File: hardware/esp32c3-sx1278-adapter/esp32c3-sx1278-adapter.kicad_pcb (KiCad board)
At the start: 2 copper layers, 24 x 55 mm, 4 parts, among them J1 Conn_01x08, J2 Conn_01x08, J3 Antenna, U2 SX1278_module

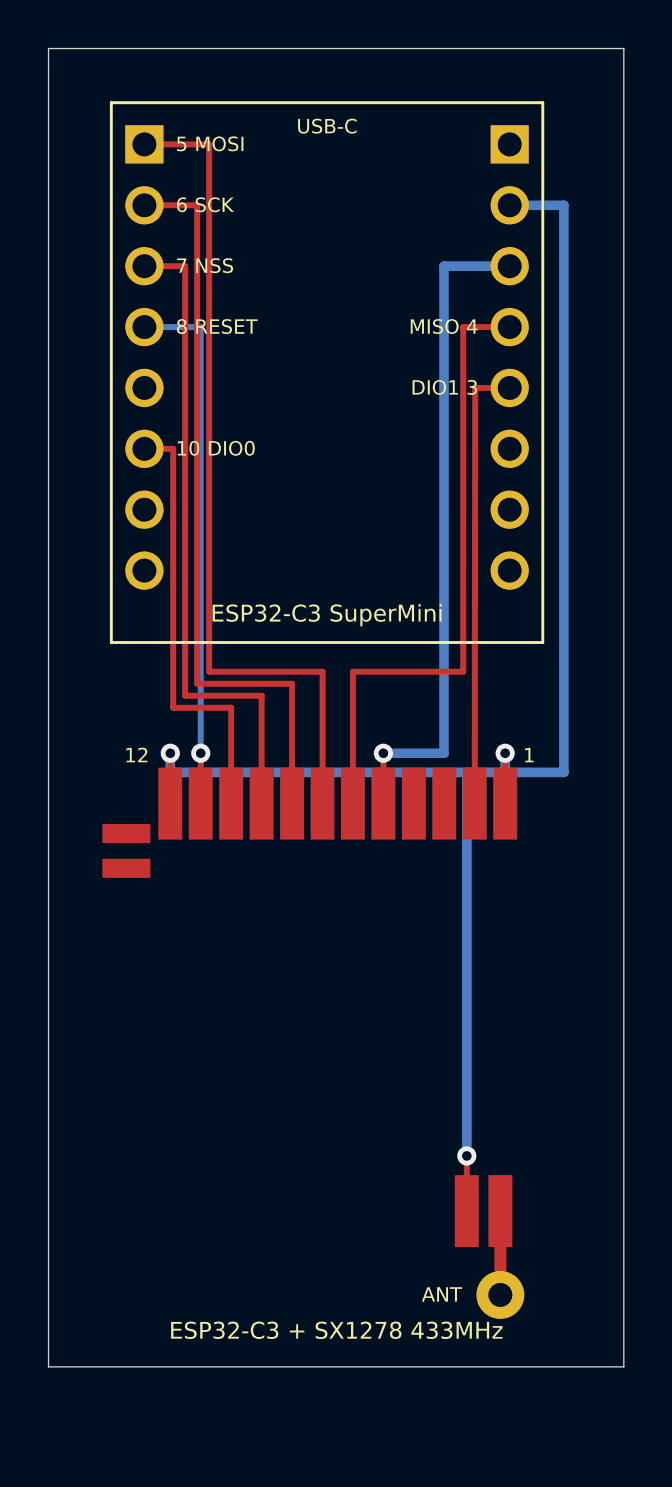
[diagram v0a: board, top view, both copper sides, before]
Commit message: Make the CC1101 adapter single-sided; add ESP32 pin names to silk
All tracks of the ESP32-C3 to CC1101 adapter now run on B.Cu (the
front keeps only the through-hole pad rings).  To make the eight nets
planar without jumpers the SuperMini lies on its side with USB-C off
the left edge, so its GPIO row sits above the socket and its power row
behind it; MISO and GDO2 go over the top of the power row and down the
left edge.  Board is 30 x 38 mm.

Both adapters now print the SuperMini's own pin names on the outer
side of each header row and the radio signal names on the inner side.
Layout plots now include B.Cu.

Co-Authored-By: Claude Fable 5.1 <noreply@anthropic.com>
Claude-Session: https://claude.ai/code/session_01JoGdh4Cg3VtTTDZi4gQuiN
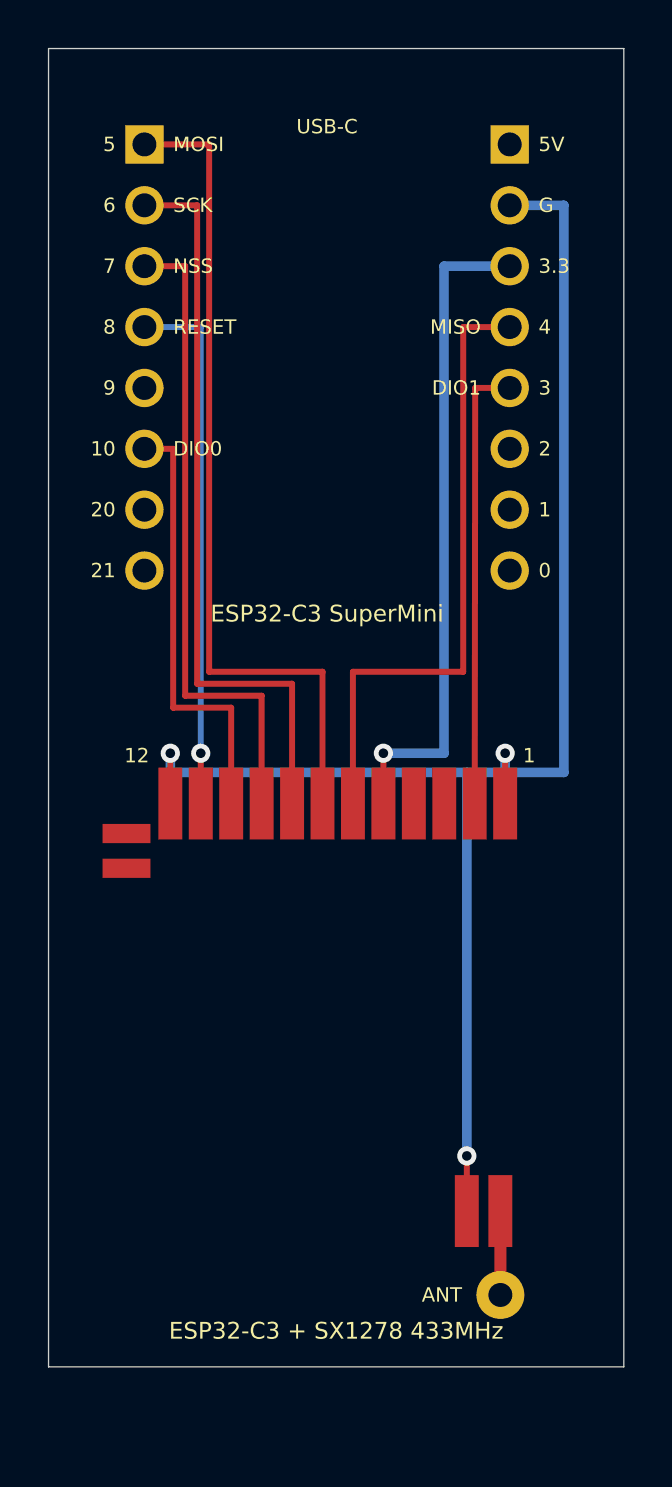
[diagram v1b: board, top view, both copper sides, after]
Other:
- board text added: "0"
- board text added: "1"
- board text added: "10"
- board text added: "2"
- board text added: "20"
- board text added: "21"
- board text added: "3"
- board text added: "3.3"
- board text added: "4"
- board text added: "5"
- board text added: "5V"
- board text added: "6"
- board text added: "7"
- board text added: "8"
- board text added: "9"
- board text added: "DIO0"
- board text added: "DIO1"
- board text added: "G"
- board text added: "MISO"
- board text added: "MOSI"
- board text added: "NSS"
- board text added: "RESET"
- board text added: "SCK"
- board text removed: "10 DIO0"
- board text removed: "5 MOSI"
- board text removed: "6 SCK"
- board text removed: "7 NSS"
- board text removed: "8 RESET"
- board text removed: "DIO1 3"
- board text removed: "MISO 4"
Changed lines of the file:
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@@
 		)
 		(fill no)
-		(layer "F.SilkS")
+		(layer "F.Fab")
 	)
 	(gr_rect
@@
 		)
 	)
-	(gr_text "5 MOSI"
-		(at 105.3 104 0)
-		(layer "F.SilkS")
-		(effects
-			(font
-				(size 0.6 0.6)
-				(thickness 0.09)
-			)
-			(justify left)
-		)
-	)
-	(gr_text "6 SCK"
-		(at 105.3 106.54 0)
-		(layer "F.SilkS")
-		(effects
-			(font
-				(size 0.6 0.6)
-				(thickness 0.09)
-			)
-			(justify left)
-		)
-	)
-	(gr_text "7 NSS"
-		(at 105.3 109.08 0)
-		(layer "F.SilkS")
-		(effects
-			(font
-				(size 0.6 0.6)
-				(thickness 0.09)
-			)
-			(justify left)
-		)
-	)
-	(gr_text "8 RESET"
-		(at 105.3 111.62 0)
-		(layer "F.SilkS")
-		(effects
-			(font
-				(size 0.6 0.6)
-				(thickness 0.09)
-			)
-			(justify left)
-		)
-	)
-	(gr_text "10 DIO0"
-		(at 105.3 116.7 0)
-		(layer "F.SilkS")
-		(effects
-			(font
-				(size 0.6 0.6)
-				(thickness 0.09)
-			)
-			(justify left)
-		)
-	)
-	(gr_text "MISO 4"
-		(at 117.94 111.62 0)
-		(layer "F.SilkS")
-		(effects
-			(font
-				(size 0.6 0.6)
-				(thickness 0.09)
-			)
-			(justify right)
-		)
-	)
-	(gr_text "DIO1 3"
-		(at 117.94 114.16 0)
-		(layer "F.SilkS")
-		(effects
-			(font
-				(size 0.6 0.6)
-				(thickness 0.09)
-			)
-			(justify right)
-		)
-	)
+	(gr_text "5"
+		(at 102.8 104 0)
+		(layer "F.SilkS")
+		(effects
+			(font
+				(size 0.6 0.6)
+				(thickness 0.09)
+			)
+			(justify right)
+		)
+	)
+	(gr_text "MOSI"
+		(at 105.2 104 0)
+		(layer "F.SilkS")
+		(effects
+			(font
+				(size 0.6 0.6)
+				(thickness 0.09)
+			)
+			(justify left)
+		)
+	)
+	(gr_text "6"
+		(at 102.8 106.54 0)
+		(layer "F.SilkS")
+		(effects
+			(font
+				(size 0.6 0.6)
+				(thickness 0.09)
+			)
+			(justify right)
+		)
+	)
+	(gr_text "SCK"
+		(at 105.2 106.54 0)
+		(layer "F.SilkS")
+		(effects
+			(font
+				(size 0.6 0.6)
+				(thickness 0.09)
+			)
+			(justify left)
+		)
+	)
+	(gr_text "7"
+		(at 102.8 109.08 0)
+		(layer "F.SilkS")
+		(effects
+			(font
+				(size 0.6 0.6)
+				(thickness 0.09)
+			)
+			(justify right)
+		)
+	)
+	(gr_text "NSS"
+		(at 105.2 109.08 0)
+		(layer "F.SilkS")
+		(effects
+			(font
+				(size 0.6 0.6)
+				(thickness 0.09)
+			)
+			(justify left)
+		)
+	)
+	(gr_text "8"
+		(at 102.8 111.62 0)
+		(layer "F.SilkS")
+		(effects
+			(font
+				(size 0.6 0.6)
+				(thickness 0.09)
+			)
+			(justify right)
+		)
+	)
+	(gr_text "RESET"
+		(at 105.2 111.62 0)
+		(layer "F.SilkS")
+		(effects
+			(font
+				(size 0.6 0.6)
+				(thickness 0.09)
+			)
+			(justify left)
+		)
+	)
+	(gr_text "9"
+		(at 102.8 114.16 0)
+		(layer "F.SilkS")
+		(effects
+			(font
+				(size 0.6 0.6)
+				(thickness 0.09)
+			)
+			(justify right)
+		)
+	)
+	(gr_text "10"
+		(at 102.8 116.7 0)
+		(layer "F.SilkS")
+		(effects
+			(font
+				(size 0.6 0.6)
+				(thickness 0.09)
+			)
+			(justify right)
+		)
+	)
+	(gr_text "DIO0"
+		(at 105.2 116.7 0)
+		(layer "F.SilkS")
+		(effects
+			(font
+				(size 0.6 0.6)
+				(thickness 0.09)
+			)
+			(justify left)
+		)
+	)
+	(gr_text "20"
+		(at 102.8 119.24 0)
+		(layer "F.SilkS")
+		(effects
+			(font
+				(size 0.6 0.6)
+				(thickness 0.09)
+			)
+			(justify right)
+		)
+	)
+	(gr_text "21"
+		(at 102.8 121.78 0)
+		(layer "F.SilkS")
+		(effects
+			(font
+				(size 0.6 0.6)
+				(thickness 0.09)
+			)
+			(justify right)
+		)
+	)
+	(gr_text "5V"
+		(at 120.44 104 0)
+		(layer "F.SilkS")
+		(effects
+			(font
+				(size 0.6 0.6)
+				(thickness 0.09)
+			)
+			(justify left)
+		)
+	)
+	(gr_text "G"
+		(at 120.44 106.54 0)
+		(layer "F.SilkS")
+		(effects
+			(font
+				(size 0.6 0.6)
+				(thickness 0.09)
+			)
+			(justify left)
+		)
+	)
+	(gr_text "3.3"
+		(at 120.44 109.08 0)
+		(layer "F.SilkS")
+		(effects
+			(font
+				(size 0.6 0.6)
+				(thickness 0.09)
+			)
+			(justify left)
+		)
+	)
+	(gr_text "4"
+		(at 120.44 111.62 0)
+		(layer "F.SilkS")
+		(effects
+			(font
+				(size 0.6 0.6)
+				(thickness 0.09)
+			)
+			(justify left)
+		)
+	)
+	(gr_text "MISO"
+		(at 118.04 111.62 0)
+		(layer "F.SilkS")
+		(effects
+			(font
+				(size 0.6 0.6)
+				(thickness 0.09)
+			)
+			(justify right)
+		)
+	)
+	(gr_text "3"
+		(at 120.44 114.16 0)
+		(layer "F.SilkS")
+		(effects
+			(font
+				(size 0.6 0.6)
+				(thickness 0.09)
+			)
+			(justify left)
+		)
+	)
+	(gr_text "DIO1"
+		(at 118.04 114.16 0)
+		(layer "F.SilkS")
+		(effects
+			(font
+				(size 0.6 0.6)
+				(thickness 0.09)
+			)
+			(justify right)
+		)
+	)
+	(gr_text "2"
+		(at 120.44 116.7 0)
+		(layer "F.SilkS")
+		(effects
+			(font
+				(size 0.6 0.6)
+				(thickness 0.09)
+			)
+			(justify left)
+		)
+	)
+	(gr_text "1"
+		(at 120.44 119.24 0)
+		(layer "F.SilkS")
+		(effects
+			(font
+				(size 0.6 0.6)
+				(thickness 0.09)
+			)
+			(justify left)
+		)
+	)
+	(gr_text "0"
+		(at 120.44 121.78 0)
+		(layer "F.SilkS")
+		(effects
+			(font
+				(size 0.6 0.6)
+				(thickness 0.09)
+			)
+			(justify left)
+		)
+	)

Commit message: CC1101 adapter GND pour with antenna keepout; optional SMA on the SX1278 adapter
* kicadgen: Zone (copper pour / keepout) support, board revision "0" in
  every title block, KICAD_SHARE overridable for non-snap installs.
* scripts/fill_zones.py: fills zones with KiCad's own filler (pcbnew python,
  re-executed inside the snap when needed) and splices only the fill
  polygons into the generated file, so generation stays reproducible.
* CC1101 adapter: GND pour on F.Cu (all tracks remain on B.Cu), keepout on
  both layers under the SuperMini's ceramic antenna; MISO/GDO2 now run
  outside the SuperMini body instead of under its antenna.
* SX1278 adapter: 24 x 58 mm, optional edge-mount SMA jack (J4) on the
  bottom edge fed from the wire-hole antenna trace, ground legs on B.Cu
  with vias to the front pads.

Co-Authored-By: Claude Fable 5.1 <noreply@anthropic.com>
Claude-Session: https://claude.ai/code/session_01JoGdh4Cg3VtTTDZi4gQuiN
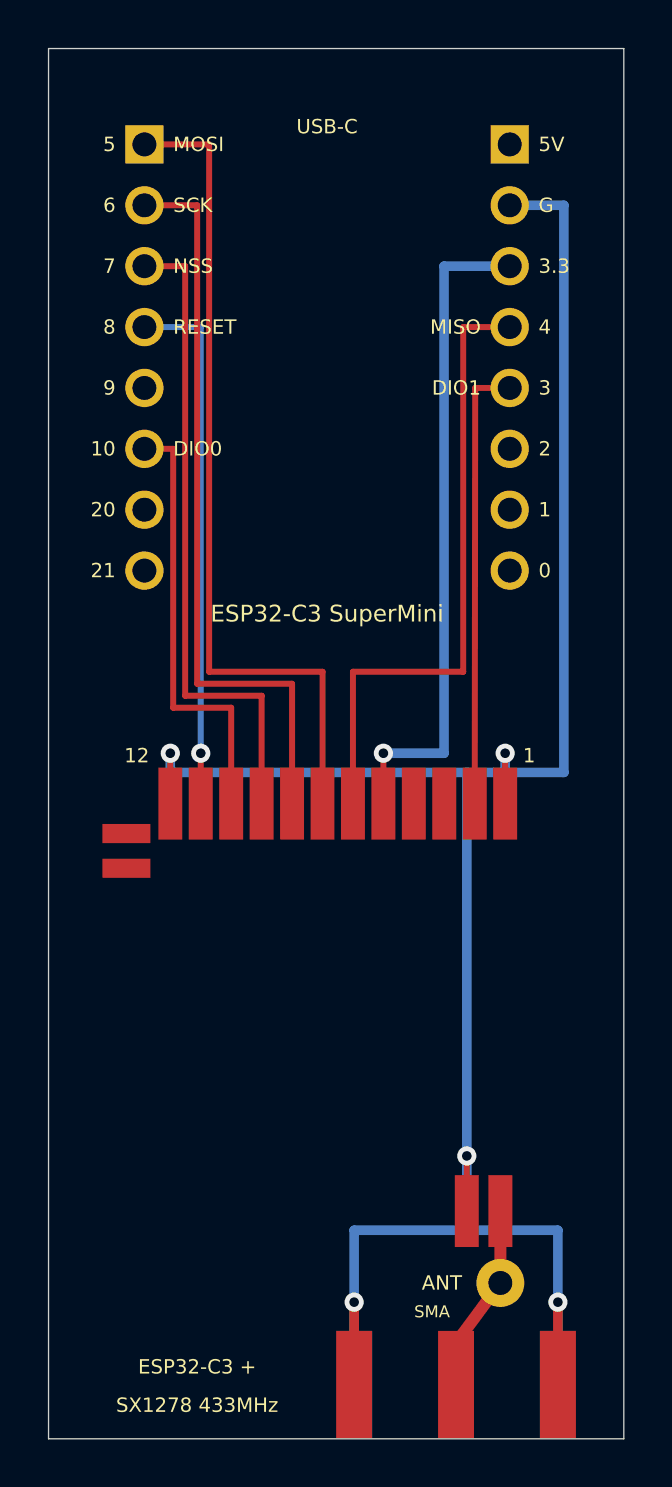
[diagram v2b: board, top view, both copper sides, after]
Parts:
- added J4: SMA, Adapter:SMA_EdgeMount_E07, F.Cu at (117.0, 158.0)
- moved J3 0.50 mm to (118.8, 151.5)
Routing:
- net GND: track 67.9 -> 99.3 mm, vias 3 -> 5
- net ANT: track 3.00 -> 7.36 mm
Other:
- board size 24 x 55 mm -> 24 x 58 mm
- board text added: "ESP32-C3 +"
- board text added: "SMA"
- board text added: "SX1278 433MHz"
- board text removed: "ESP32-C3 + SX1278 433MHz"
